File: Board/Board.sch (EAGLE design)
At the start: 51 parts, among them IC1 NJM4556, J1 POWER_JACKPTH, X1 RCA-4-117-01

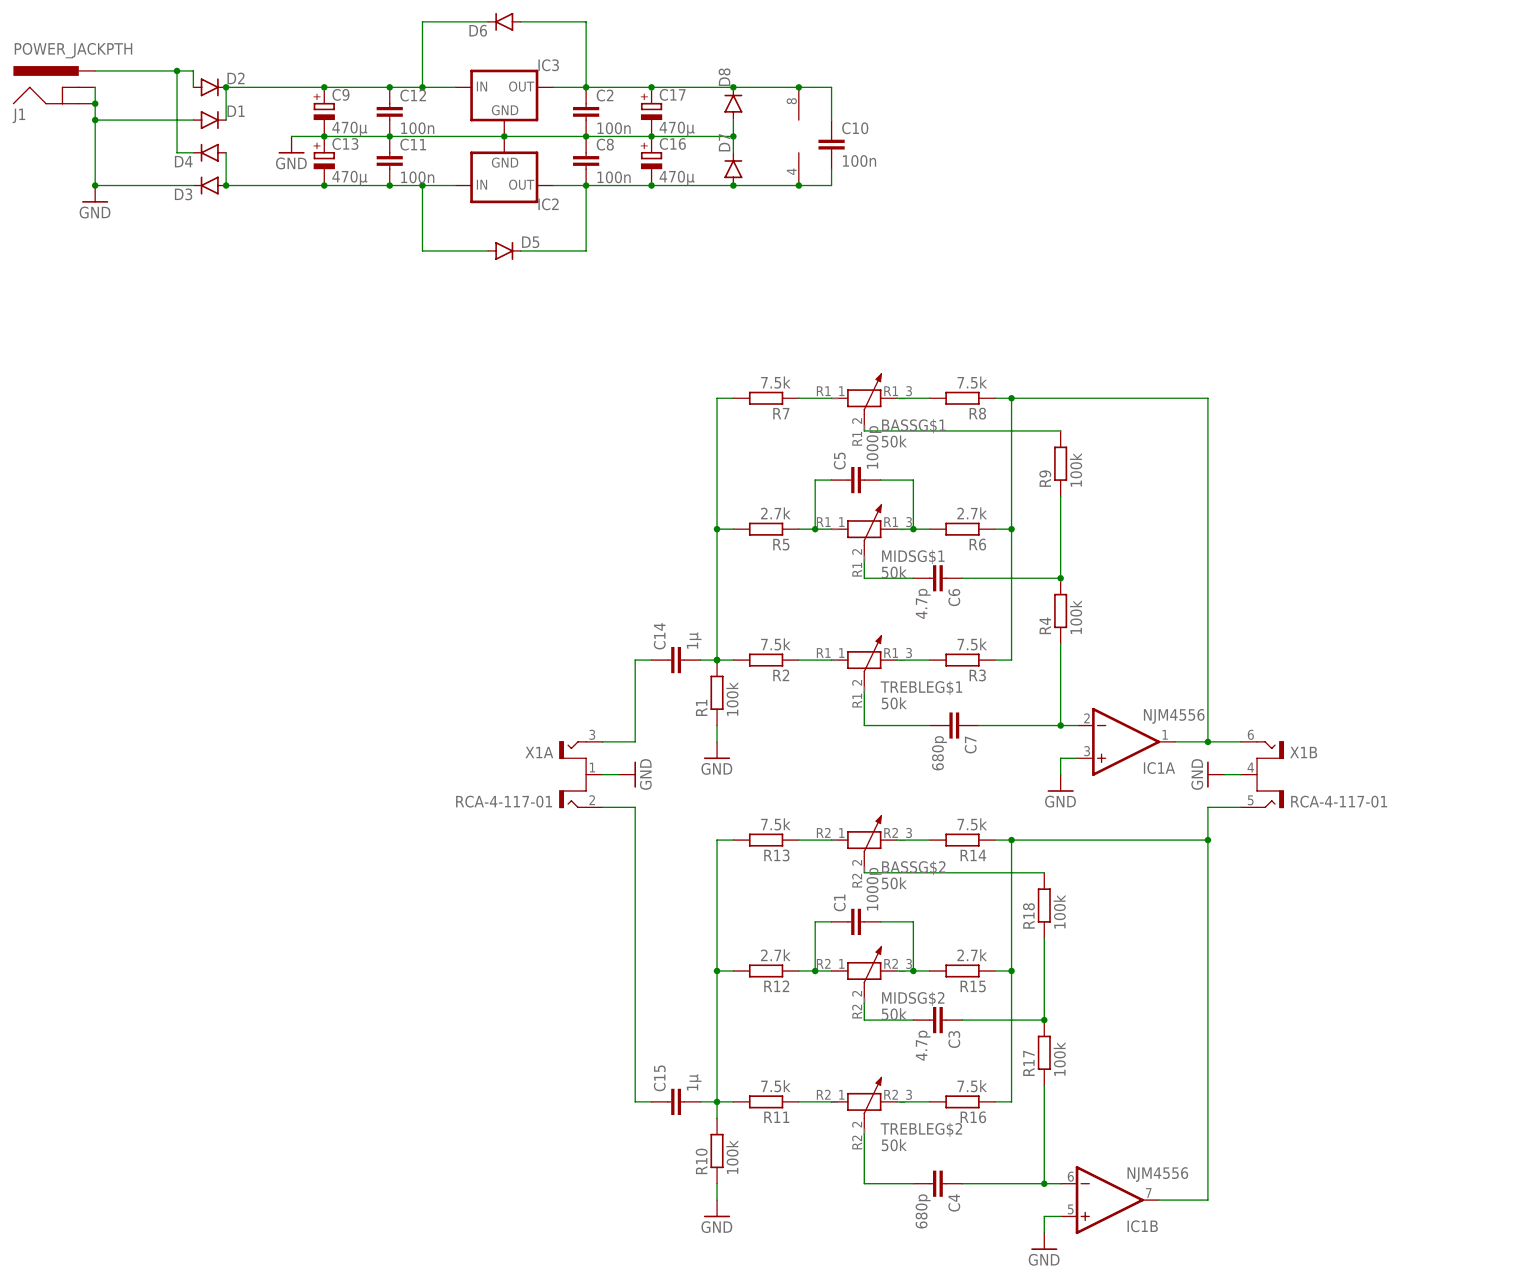
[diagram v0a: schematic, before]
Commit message: added switch on delay via relay and 555 circuit
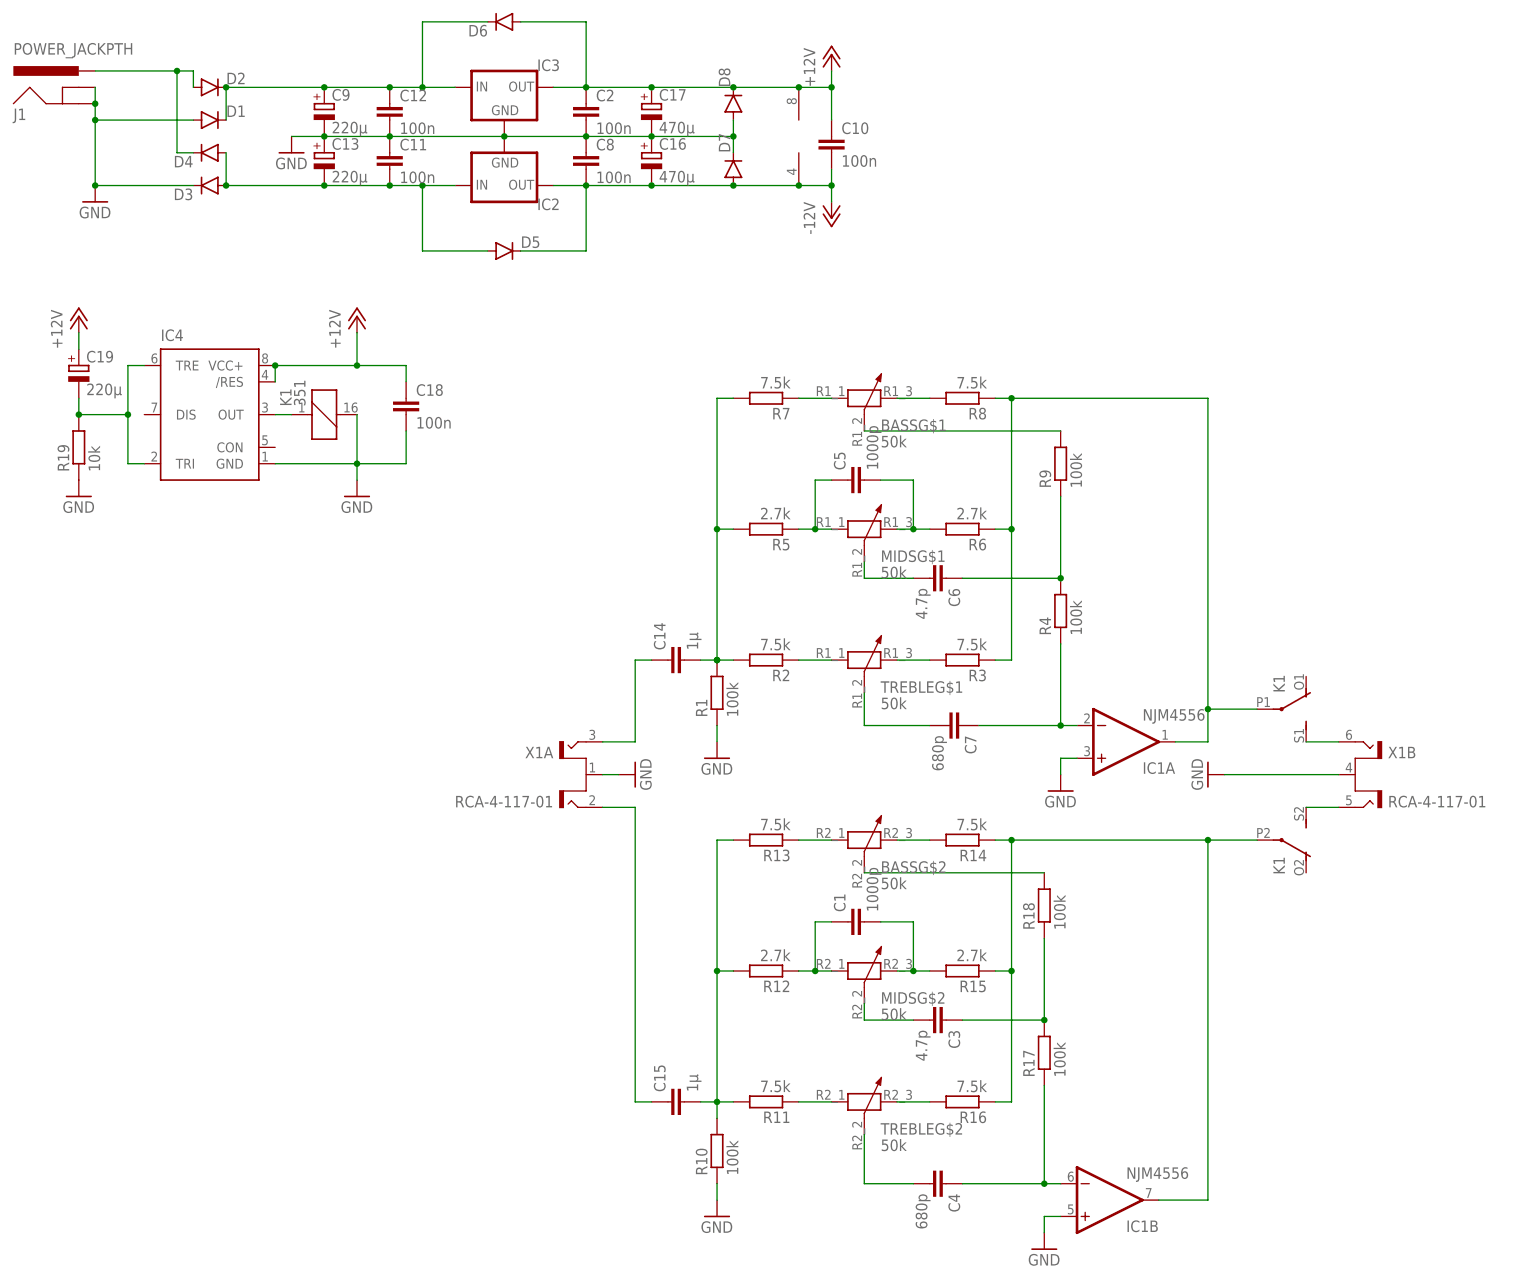
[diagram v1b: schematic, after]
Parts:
- added C18: 100n, rcl:C-EUC0603
- added C19: 220µ, rcl:CPOL-EU175TMP-0810
- added IC4: (no value), SparkFun-AnalogIC:NE555D
- added K1: 351, relay:351
- added R19: 10k, rcl:R-EU_R1206
- C13, C9: value 470µ -> 220µ
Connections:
- net N$27 renamed -12V
- new net +12V: C10.1, C17.+, C18.1, C19.+, C2.1, D6.A, D8.C, IC1P.V+, IC3.OUT, IC4./RES, IC4.VCC+
- new net N$13: K12.S, X1B.T2
- new net N$25: K13.S, X1B.T1
- new net N$26: C19.-, IC4.TRE, IC4.TRI, R19.2
- net GND: now also C18.2, IC4.GND, K11.2, R19.1
- net N$30: now also IC4.OUT, K11.1; no longer C10.1, C17.+, C2.1, D6.A, D8.C, IC1P.V+, IC3.OUT
- net OUT_L: now also K13.P; no longer X1B.T1
- net OUT_R: now also K12.P; no longer X1B.T2
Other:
- moved on the sheet: X1B

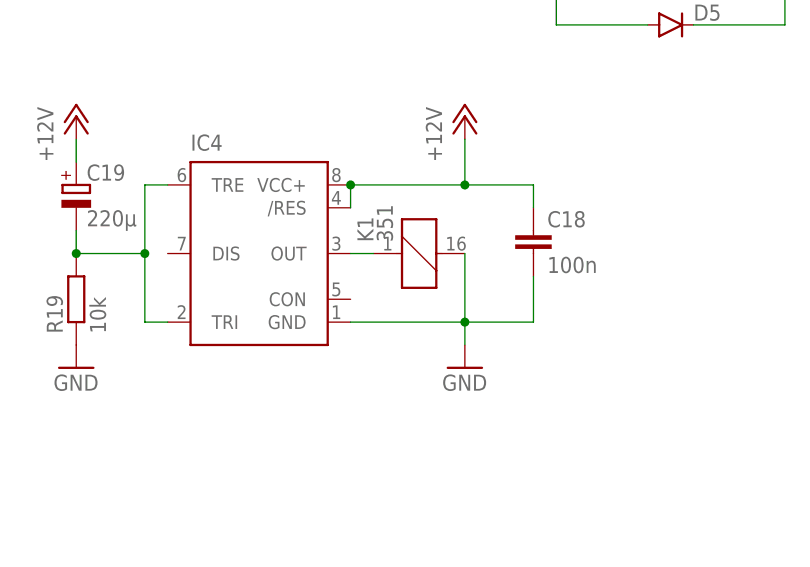
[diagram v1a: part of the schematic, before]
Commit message: added missing flyback diode to relay
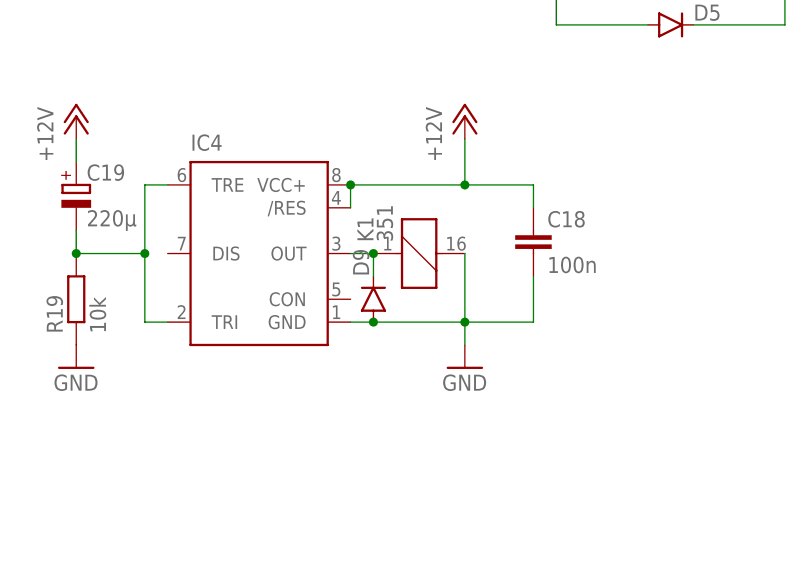
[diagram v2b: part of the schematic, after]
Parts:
- added D9: (no value), SparkFun-DiscreteSemi:DIODEBAS16
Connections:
- net GND: now also D9.A
- net N$30: now also D9.C
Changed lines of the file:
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@@
 <part name="GND10" library="supply1" library_urn="urn:adsk.eagle:library:371" deviceset="GND" device=""/>
 <part name="C18" library="rcl" library_urn="urn:adsk.eagle:library:334" deviceset="C-EU" device="C0603" package3d_urn="urn:adsk.eagle:package:23616/2" value="100n"/>
+<part name="D9" library="SparkFun-DiscreteSemi" deviceset="DIODE" device="BAS16"/>
 </parts>
 <sheets>
@@
 <instance part="GND10" gate="1" x="-5.08" y="104.14"/>
 <instance part="C18" gate="G$1" x="45.72" y="119.38"/>
+<instance part="D9" gate="G$1" x="27.94" y="111.76" rot="R90"/>
 </instances>
 <busses>
@@
 <segment>
 <pinref part="IC4" gate="G$1" pin="GND"/>
-<wire x1="25.4" y1="109.22" x2="38.1" y2="109.22" width="0.1524" layer="91"/>
+<wire x1="25.4" y1="109.22" x2="27.94" y2="109.22" width="0.1524" layer="91"/>
 <pinref part="GND9" gate="1" pin="GND"/>
+<wire x1="27.94" y1="109.22" x2="38.1" y2="109.22" width="0.1524" layer="91"/>
 <wire x1="38.1" y1="106.68" x2="38.1" y2="109.22" width="0.1524" layer="91"/>
 <pinref part="K1" gate="1" pin="2"/>
@@
 <wire x1="45.72" y1="114.3" x2="45.72" y2="109.22" width="0.1524" layer="91"/>
 <wire x1="45.72" y1="109.22" x2="38.1" y2="109.22" width="0.1524" layer="91"/>
+<pinref part="D9" gate="G$1" pin="A"/>
+<junction x="27.94" y="109.22"/>
 </segment>
 <segment>
@@
 <pinref part="K1" gate="1" pin="1"/>
 <wire x1="25.4" y1="116.84" x2="27.94" y2="116.84" width="0.1524" layer="91"/>
-</segment>
-</net>
+<pinref part="D9" gate="G$1" pin="C"/>
+<wire x1="27.94" y1="116.84" x2="27.94" y2="114.3" width="0.1524" layer="91"/>
+<junction x="27.94" y="116.84"/>
+</segment>
+</net>

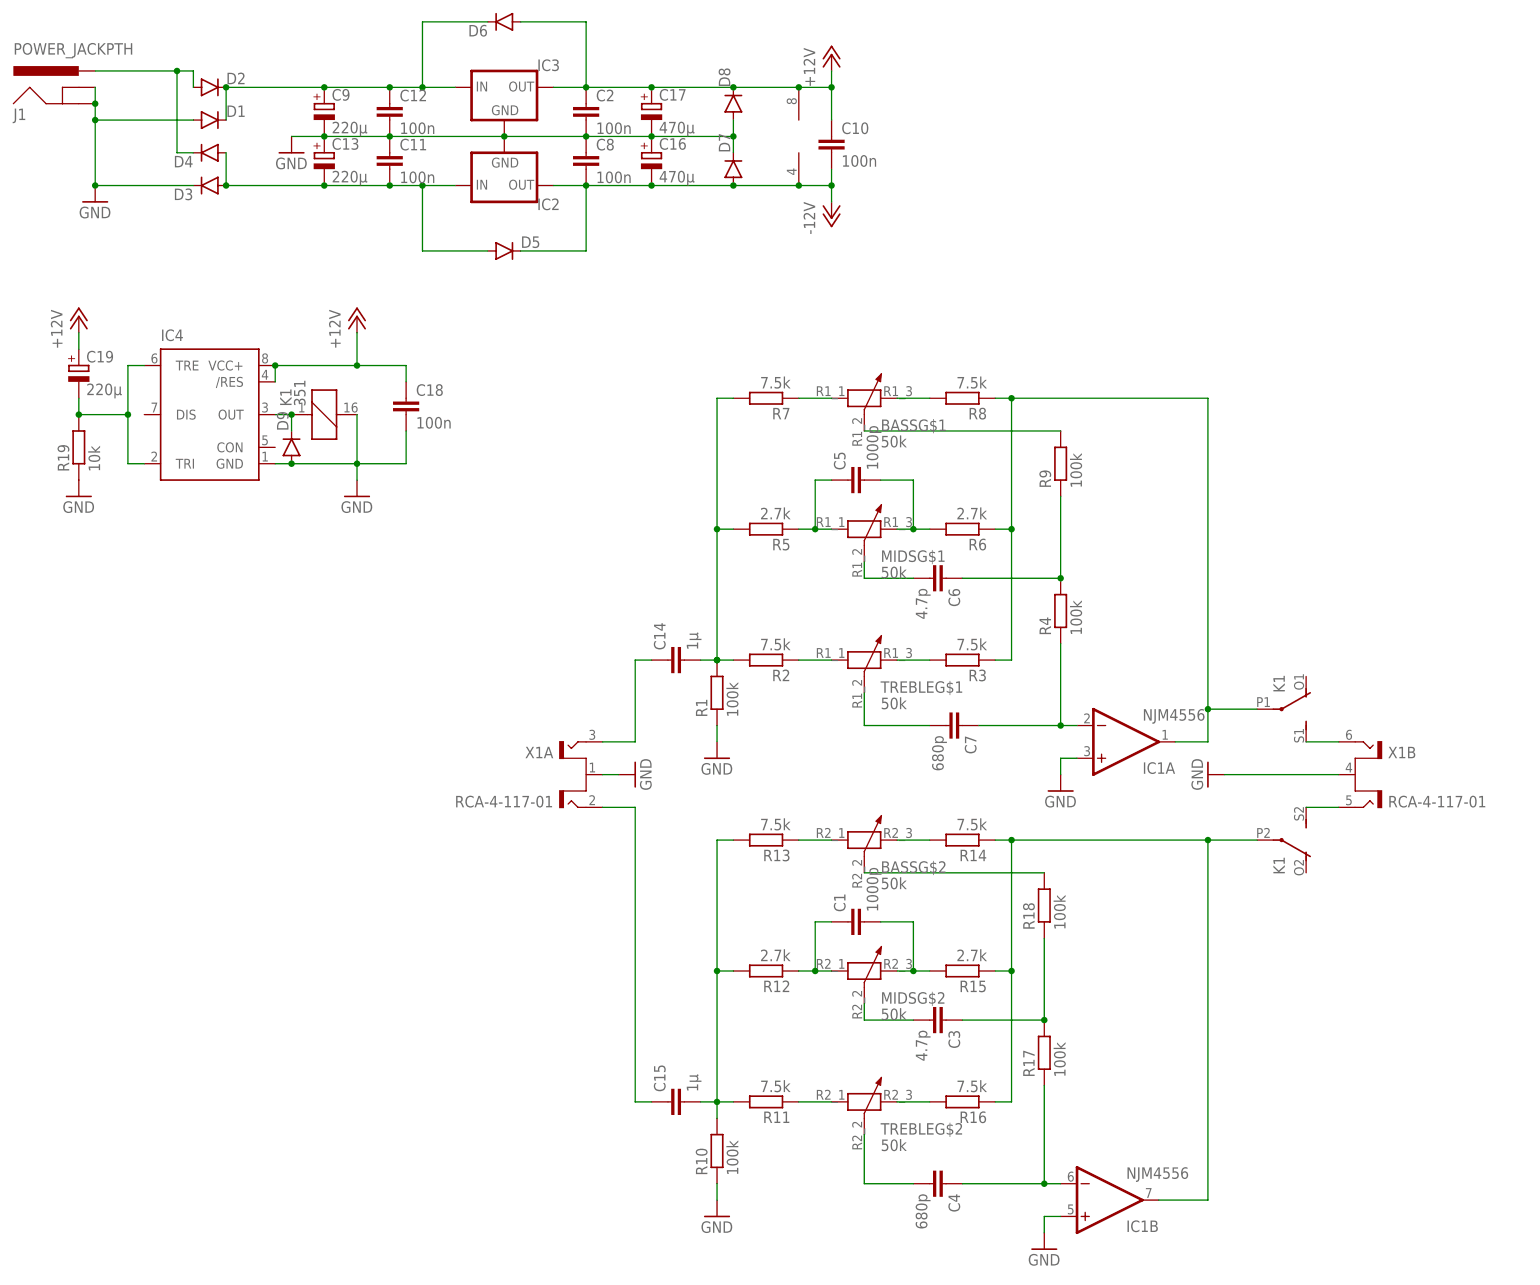
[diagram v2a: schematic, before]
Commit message: fixed orientation issue with pots
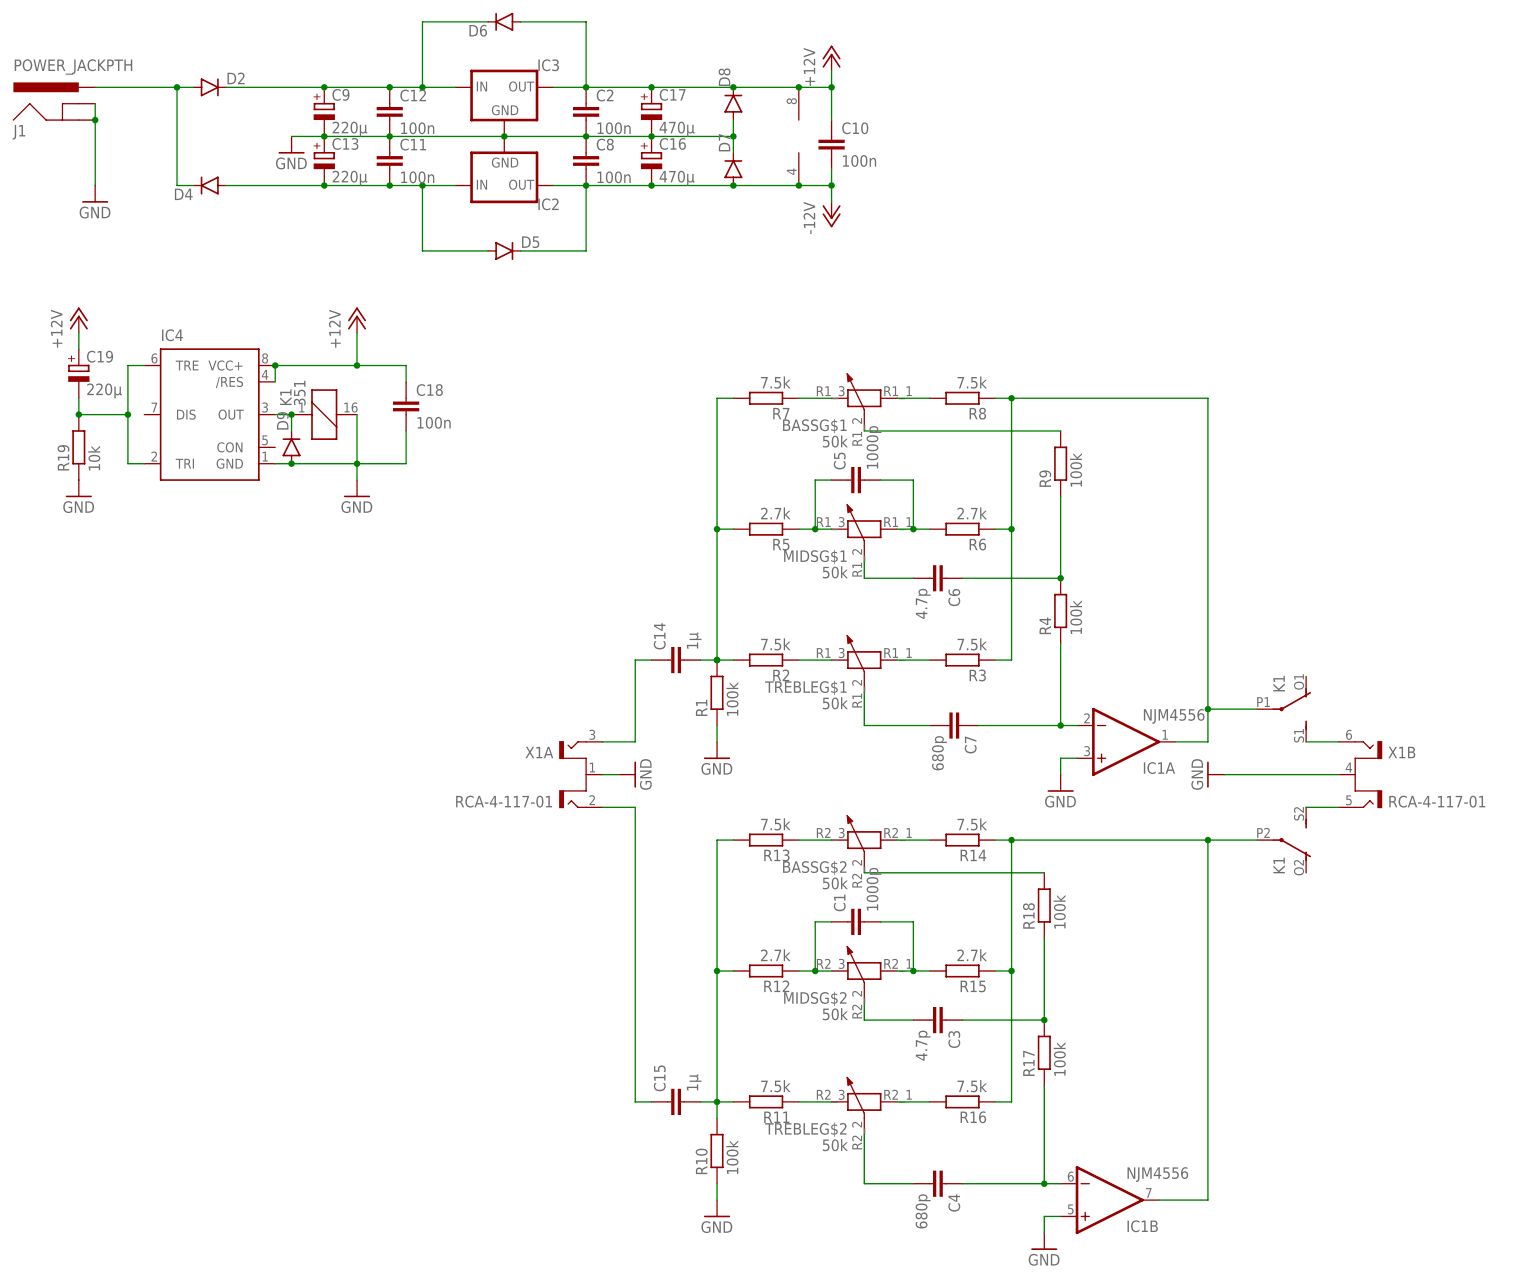
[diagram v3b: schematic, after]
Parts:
- removed D1, D3: (no value), SparkFun-DiscreteSemi:DIODEBAS16
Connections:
- net GND: no longer D1.A, D3.C
- net N$10: now also BASSG$2.2, R13.1; no longer R11.1, TREBLEG$2.1
- net N$15: now also MIDSG$1.1; no longer MIDSG$1.2
- net N$18: now also BASSG$2.1, R14.2; no longer R16.2, TREBLEG$2.2
- net N$19: now also MIDSG$2.2; no longer MIDSG$2.1
- net N$2: now also TREBLEG$1.2; no longer TREBLEG$1.1
- net N$20: now also MIDSG$2.1; no longer MIDSG$2.2
- net N$21: now also R11.1, TREBLEG$2.2; no longer BASSG$2.1, R13.1
- net N$22: now also R16.2, TREBLEG$2.1; no longer BASSG$2.2, R14.2
- net N$23: no longer D3.A
- net N$24: no longer D1.C
- net N$4: now also TREBLEG$1.1; no longer TREBLEG$1.2
- net N$5: now also MIDSG$1.2; no longer MIDSG$1.1
- net N$7: now also BASSG$1.2; no longer BASSG$1.1
- net N$8: now also BASSG$1.1; no longer BASSG$1.2
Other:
- moved on the sheet: D4, J1
